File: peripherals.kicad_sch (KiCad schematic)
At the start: 53 parts, among them J10 533980471, J11 ERF8-040-05.0-L-DV-K-TR, J7 FC Conn, J9 TC2050-IDC-NL, Q10 PJE138K, Q9 PJE138K, U30 TPD4E05U06QDQARQ1, U33 NTS0102GT, U34 PCAL6408ABSHP

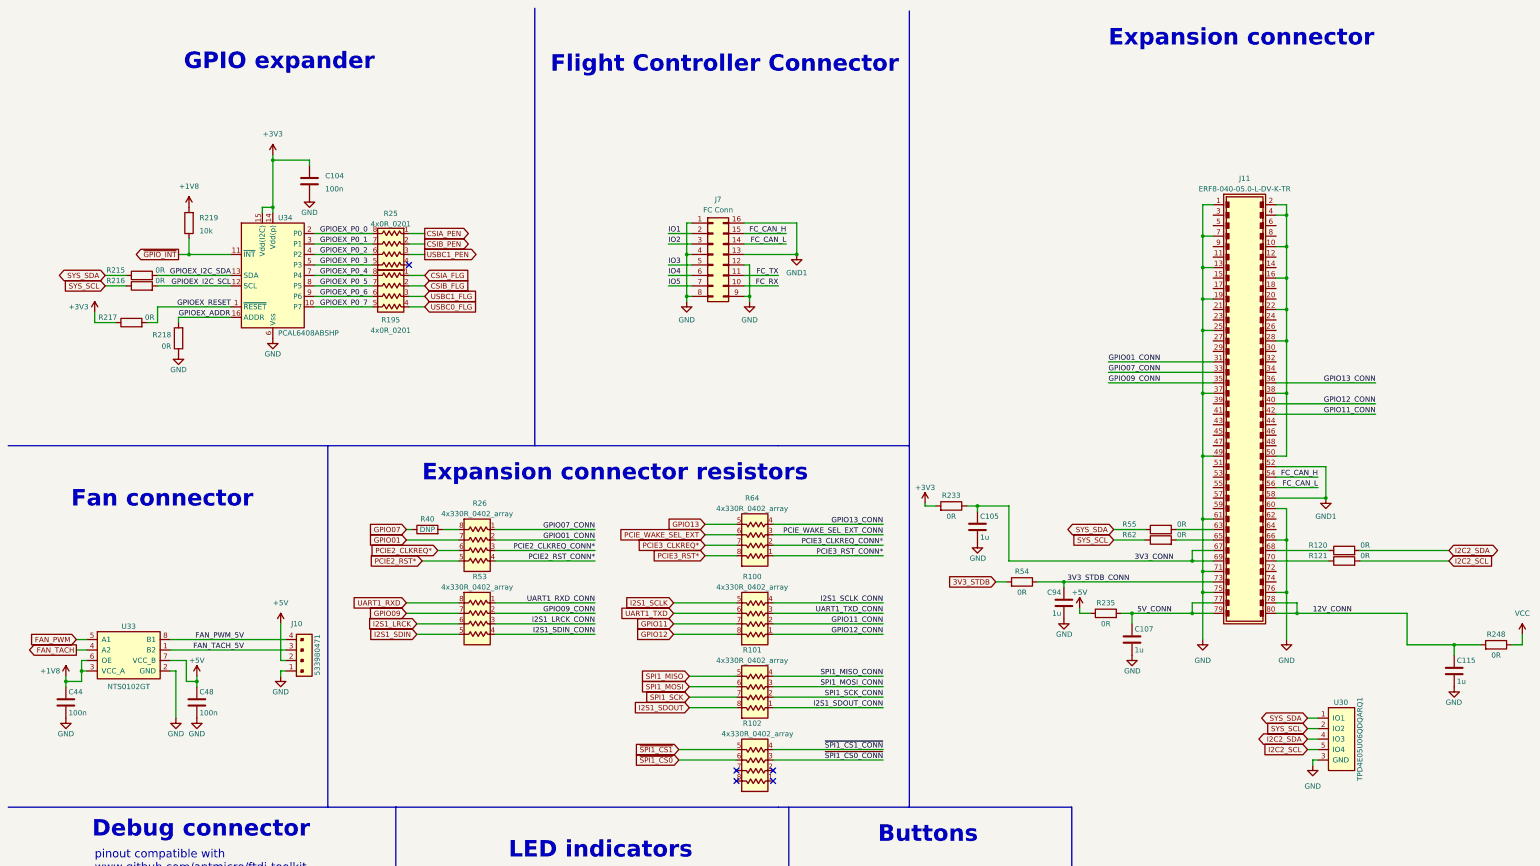
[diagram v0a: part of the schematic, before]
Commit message: Reducing pin count to 30
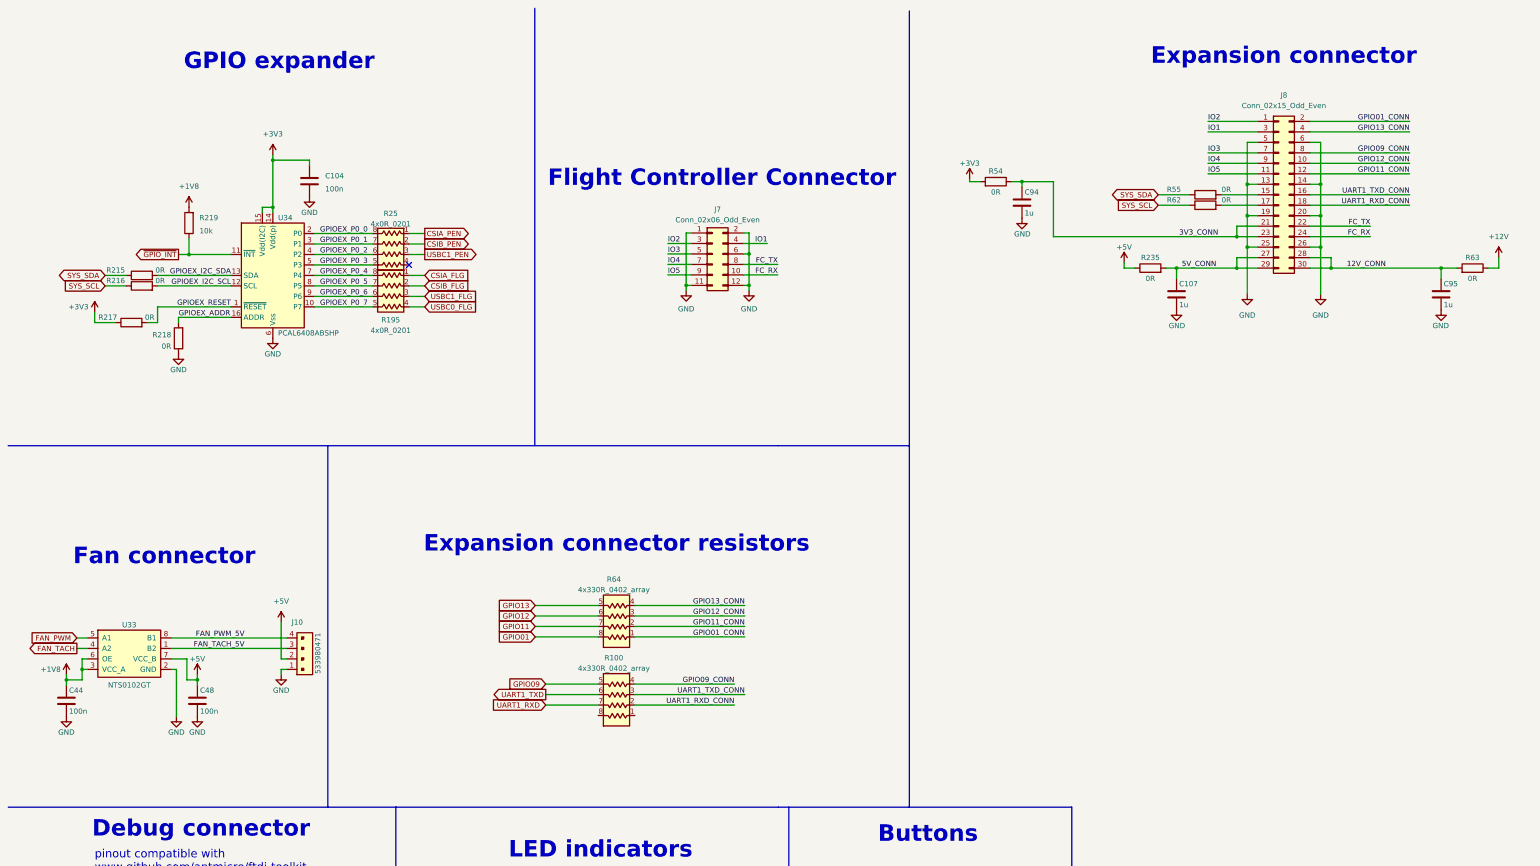
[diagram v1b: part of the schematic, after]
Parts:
- removed C105, C115: C_1u_0402, jetson-orin-baseboard-footprints:0402-cap, symbol jetson-orin-baseboard:C_1u_0402
- removed J11: ERF8-040-05.0-L-DV-K-TR, jetson-orin-baseboard-footprints:ERF8-040-XX.X-X-DV-XX, symbol jetson-orin-baseboard:ERF8-040-05.0-L-DV-K-TR
- removed J7: FC Conn, symbol Connector_Generic:Conn_02x08_Counter_Clockwise
- removed R101, R102, R26, R53: 4x330R_0402_array, jetson-orin-baseboard-footprints:R_Array_4x0402, symbol jetson-orin-baseboard:4x330R_0402_array
- removed R120, R121: R_0R_0402, jetson-orin-baseboard-footprints:0402-res, symbol jetson-orin-baseboard:R_0R_0402
- removed R233, R248: R_0R_0603, jetson-orin-baseboard-footprints:0603-res, symbol jetson-orin-baseboard:R_0R_0603
- removed R40: DNP, symbol Device:R
- removed U30: TPD4E05U06QDQARQ1, jetson-orin-baseboard-footprints:USON-10_2.5x1.0mm_P0.5mm, symbol jetson-orin-baseboard:TPD4E05U06QDQARQ1
- added C95: C_1u_0402, jetson-orin-baseboard-footprints:0402-cap, symbol jetson-orin-baseboard:C_1u_0402
- added J7: Conn_02x06_Odd_Even, symbol Connector_Generic:Conn_02x06_Odd_Even
- added J8: Conn_02x15_Odd_Even, symbol Connector_Generic:Conn_02x15_Odd_Even
- added R63: R_0R_0603, jetson-orin-baseboard-footprints:0603-res, symbol jetson-orin-baseboard:R_0R_0603
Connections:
- net 3V3_STDB is gone; now on net +3V3: R54.2
- net 3V3_STDB_CONN is gone; now on net 3V3_CONN: C94.1, R54.1
- net I2S1_SCLK is gone; now on net GPIO09: R100.5
- net I2S1_SCLK_CONN is gone; now on net GPIO09_CONN: R100.4
- net PCIE3_CLKREQ* is gone; now on net GPIO11: R64.7
- net PCIE3_CLKREQ_CONN* is gone; now on net GPIO11_CONN: R64.2
- net PCIE3_RST* is gone; now on net GPIO01: R64.8
- net PCIE3_RST_CONN* is gone; now on net GPIO01_CONN: R64.1
- net PCIE_WAKE_SEL_EXT is gone; now on net GPIO12: R64.6
- net PCIE_WAKE_SEL_EXT_CONN is gone; now on net GPIO12_CONN: R64.3
- net 12V_CONN: now also C95.1, J8.28 (Pin_28), J8.30 (Pin_30), R63.2
- net 3V3_CONN: now also J8.21 (Pin_21), J8.23 (Pin_23)
- net 5V_CONN: now also J8.27 (Pin_27), J8.29 (Pin_29)
- net FC_RX: now also J7.10 (Pin_10), J8.24 (Pin_24)
- net FC_TX: now also J7.8 (Pin_8), J8.22 (Pin_22)
- net GND: now also C95.2, J7.1 (Pin_1), J7.11 (Pin_11), J7.12 (Pin_12), J7.2 (Pin_2), J7.6 (Pin_6), J8.13 (Pin_13), J8.14 (Pin_14), J8.19 (Pin_19), J8.20 (Pin_20), J8.25 (Pin_25), J8.26 (Pin_26), J8.5 (Pin_5), J8.6 (Pin_6)
- net GPIO01_CONN: now also J8.2 (Pin_2)
- net GPIO09_CONN: now also J8.8 (Pin_8)
- net GPIO11: no longer R100.7
- net GPIO11_CONN: now also J8.12 (Pin_12); no longer R100.2
- net GPIO12: no longer R100.8
- net GPIO12_CONN: now also J8.10 (Pin_10); no longer R100.1
- net GPIO13_CONN: now also J8.4 (Pin_4)
- net IO1: now also J7.4 (Pin_4), J8.3 (Pin_3)
- net IO2: now also J7.3 (Pin_3), J8.1 (Pin_1)
- net IO3: now also J7.5 (Pin_5), J8.7 (Pin_7)
- net IO4: now also J7.7 (Pin_7), J8.9 (Pin_9)
- net IO5: now also J7.9 (Pin_9), J8.11 (Pin_11)
- net UART1_RXD: now also R100.7
- net UART1_RXD_CONN: now also R100.2, J8.18 (Pin_18)
- net UART1_TXD_CONN: now also J8.16 (Pin_16)
- net at R62.2: now also J8.17 (Pin_17)
- net at R55.2: now also J8.15 (Pin_15)
- new net +12V: R63.1
- no-connect marks 6 -> 2
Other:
- moved on the sheet: C107, R100, R235, R64

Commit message: Schematic check
Include Pinmux and Schematic Check excels in doc folder and doing a lot of checking and correcting things.
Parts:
- removed C104: C_100n_0402, jetson-orin-baseboard-footprints:0402-cap, symbol jetson-orin-baseboard:C_100n_0402
- removed R100: 4x330R_0402_array, jetson-orin-baseboard-footprints:R_Array_4x0402, symbol jetson-orin-baseboard:4x330R_0402_array
- removed R195, R25: 4x0R_0201_array, jetson-orin-baseboard-footprints:EXB18V, symbol jetson-orin-baseboard:4x0R_0201_array
- removed R215, R216, R217, R218: R_0R_0402, jetson-orin-baseboard-footprints:0402-res, symbol jetson-orin-baseboard:R_0R_0402
- removed R219: R_10k_0402, jetson-orin-baseboard-footprints:0402-res, symbol jetson-orin-baseboard:R_10k_0402
- removed U34: PCAL6408ABSHP, jetson-orin-baseboard-footprints:VQFN-16-1EP_3x3mm, symbol jetson-orin-baseboard:PCAL6408ABSHP
- added C42, C43: 100n, symbol Device:C
- added C79: 0.1u, symbol Device:C
- added C80: 2.2u, symbol Device:C
- added C81: 10n, symbol Device:C
- added C82: 0.47u, symbol Device:C
- added C88: C_1u_0402, jetson-orin-baseboard-footprints:0402-cap, symbol jetson-orin-baseboard:C_1u_0402
- added D14, D15, D16, D17: TPD1E0B04DPYR, jetson-orin-baseboard-footprints:XDFN-2_1x0.60mm, symbol jetson-orin-baseboard:TPD1E0B04DPYR
- added R1: R_0R_0603, jetson-orin-baseboard-footprints:0603-res, symbol jetson-orin-baseboard:R_0R_0603
- added R2: 0, symbol Device:R
- added U2: ICM-20602, Package_LGA:LGA-16_3x3mm_P0.5mm_LayoutBorder3x5y, symbol Sensor_Motion:ICM-20602
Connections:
- net GPIO09_CONN is gone; now on net FC_TX: J8.8 (Pin_8)
- net GPIO11 is gone; now on net UART1_RXD: R64.7
- net GPIO12 is gone; now on net UART1_TXD: R64.6
- net +1V8: now also C79.1, C80.1, R1.2, U2.16 (VDD)
- net 3V3_CONN: no longer J8.23 (Pin_23)
- net FC_RX: now also J8.10 (Pin_10); no longer J8.24 (Pin_24)
- net FC_TX: no longer J8.22 (Pin_22)
- net GND: now also C79.2, C80.2, C81.2, C82.2, C88.2, D14.2, D15.2, D16.2, D17.2, U2.10 (GND), U2.11 (GND), U2.12 (GND), U2.13 (GND), U2.15 (GND), U2.8 (FSYNC), U2.9 (GND)
- net GPIO09: now also R2.2
- net GPIO13_CONN: now also J8.12 (Pin_12); no longer J8.4 (Pin_4), R64.4
- net UART1_RXD_CONN: now also J8.4 (Pin_4), R64.2; no longer J8.18 (Pin_18)
- net UART1_TXD_CONN: now also J8.2 (Pin_2), R64.3; no longer J8.16 (Pin_16)
- net GPIO01: no longer names the net of R64.8
- net GPIO01_CONN: no longer names the net of R64.1
- net GPIO01_CONN: no longer J8.2 (Pin_2)
- removed net GPIO11_CONN: J8.12 (Pin_12), R64.2
- removed net GPIO12_CONN: J8.10 (Pin_10), R64.3
- net GPIO13 renamed GPIO_PAC
- new net: C81.1, U2.1 (VDDIO)
- new net: C82.1, U2.14 (REGOUT)
- new net: R2.1, U2.6 (INT)
- new net 1V8_CONN: C88.1, J8.23 (Pin_23), R1.1
- new net GPIO_PAC_CONN: R64.4
- new net SPIO_MISO: U2.4 (SAO/SD0)
- new net SPIO_MOSI: U2.3 (SDA/SDI)
- new net SPIO_SCK: U2.2 (SCL/SPC)
- new net USBSS1_RX_N: D14.1, J8.24 (Pin_24)
- new net USBSS1_RX_P: D15.1, J8.22 (Pin_22)
- new net USBSS1_TX_N: C43.2
- new net USBSS1_TX_N_CONN: C43.1, D17.1, J8.18 (Pin_18)
- new net USBSS1_TX_P: C42.2
- new net USBSS1_TX_P_CONN: C42.1, D16.1, J8.16 (Pin_16)
- new net ~{SPI0_CS0}: U2.5 (~{CS})
- no-connect marks 2 -> 1
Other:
- note added: "IMU"
- note added: "SYS I2C Addresses in Use -0100011 for Port 1 of I2C1 of TPS65988 (CONFIGURABLE) -0100111 for Port 2 of I2C1 of TPS65988 (CONFIGURABLE) -0010010 for TUSB1046-DCI (I2C UNUSED, CONFIGURABLE) -1X00111 for HD3SS3220(I2C UNUSED, 2 CHOICE) -010000X for planned PCAL6408A on PAC PCB (2 CHOICE) -1000000 for power monitor on module"
- note removed: "GPIO expander"
- moved on the sheet: C107, C94, C95, J8, R235, R54, R55, R62, R63, R64

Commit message: Small changes
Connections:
- net GPIO13_CONN is gone; now on net GPIO_PAC_CONN: J8.12 (Pin_12)
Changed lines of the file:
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@@
     (effects (font (size 1.27 1.27)) (justify left bottom))
   )
-  (label "GPIO13_CONN" (at 353.06 53.34 180) (fields_autoplaced)
+  (label "GPIO_PAC_CONN" (at 353.06 53.34 180) (fields_autoplaced)
     (effects (font (size 1.27 1.27)) (justify right bottom))
   )
@@
     )
   )
-  (global_label "GPIO_PAC" (shape input) (at 140.97 157.48 180) (fields_autoplaced)
+  (global_label "GPIO_PAC" (shape output) (at 140.97 157.48 180) (fields_autoplaced)
     (effects (font (size 1.27 1.27)) (justify right))
     (property "Intersheetrefs" "${INTERSHEET_REFS}" (at 128.9133 157.48 0)
@@
   (symbol (lib_id "power:GND") (at 78.105 91.44 0) (unit 1)
     (in_bom yes) (on_board yes) (dnp no) (fields_autoplaced)
-    (property "Reference" "#PWR015" (at 78.105 97.79 0)
+    (property "Reference" "#PWR020" (at 78.105 97.79 0)
       (effects (font (size 1.27 1.27)) hide)
     )
@@
   (symbol (lib_id "power:GND") (at 93.98 60.325 0) (unit 1)
     (in_bom yes) (on_board yes) (dnp no) (fields_autoplaced)
-    (property "Reference" "#PWR024" (at 93.98 66.675 0)
+    (property "Reference" "#PWR021" (at 93.98 66.675 0)
       (effects (font (size 1.27 1.27)) hide)
     )
@@
   (symbol (lib_id "power:GND") (at 62.23 64.135 0) (unit 1)
     (in_bom yes) (on_board yes) (dnp no) (fields_autoplaced)
-    (property "Reference" "#PWR023" (at 62.23 70.485 0)
-      (effects (font (size 1.27 1.27)) hide)
-    )
+    (property "Reference" "#PWR015" (at 62.23 70.485 0)
+      (effects (font (size 1.27 1.27)) hide)
+    )

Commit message: Schematic Done
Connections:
- no-connect marks 1 -> 3
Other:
- moved on the sheet: C107, C43, C44, C48, C79, C80, C81, C82, C94, D14, D15, D16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

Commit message: Schematic V1 and footprints assigned
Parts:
- removed J7: Conn_02x06_Odd_Even, symbol Connector_Generic:Conn_02x06_Odd_Even
- removed J8: Conn_02x15_Odd_Even, symbol Connector_Generic:Conn_02x15_Odd_Even
- added J10: 532611071, jetson-orin-baseboard-footprints:MOLEX_532611071, symbol 532611071:532611071
- added J11: ERF8-020-05.0-S-DV-L-TR, jetson-orin-baseboard-footprints:ERF8-040-XX.X-X-DV-XX, symbol ERF8-020-05.0-S-DV-L-TR:ERF8-020-05.0-S-DV-L-TR
- C79: footprint (none) -> jetson-orin-baseboard-footprints:0402-cap
- C81: renamed from C80; footprint (none) -> jetson-orin-baseboard-footprints:0402-cap
- C82: renamed from C81; footprint (none) -> jetson-orin-baseboard-footprints:0402-cap
- C83: renamed from C82; footprint (none) -> jetson-orin-baseboard-footprints:0402-cap
- C87: renamed from C42; footprint (none) -> jetson-orin-baseboard-footprints:0402-cap
- C89: renamed from C43; footprint (none) -> jetson-orin-baseboard-footprints:0402-cap
- R106: renamed from R2; footprint (none) -> jetson-orin-baseboard-footprints:0402-res
- renumbered C44 to C78, C48 to C80, C94 to C84, C88 to C85, C107 to C86, C95 to C88, D26 to D37, D27 to D38, D58 to D39, D59 to D40, D14 to D41, D15 to D42, D16 to D43, D17 to D44, J9 to J8, J10 to J9, Q9 to Q4, Q10 to Q5, R111 to R103, R112 to R104, R204 to R105, R222 to R107, R223 to R108, R64 to R109, R230 to R110, R231 to R111, R232 to R112, R242 to R113, R54 to R114, R1 to R115, R235 to R116, R55 to R117, R62 to R118, R63 to R119, U33 to U20, U2 to U21
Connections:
- net 12V_CONN: now also J11.32, J11.34, J11.36, J11.38
- net 1V8_CONN: now also J11.02, J11.04
- net 3V3_CONN: now also J11.33, J11.35, J11.37
- net 5V_CONN: now also J11.01, J11.03, J11.05, J11.07
- net FC_RX: now also J10.3, J11.16
- net FC_TX: now also J10.2, J11.14
- net GND: now also J10.1, J10.4, J10.8, J10.S1 (SHIELD1), J10.S2 (SHIELD2), J11.06, J11.09, J11.12, J11.17, J11.18, J11.24, J11.25, J11.30, J11.31, J11.39, J11.40
- net GPIO_PAC_CONN: now also J11.23
- net IO1: now also J10.5, J11.13
- net IO2: now also J10.6, J11.11
- net IO3: now also J10.7, J11.15
- net IO4: now also J10.9, J11.19
- net IO5: now also J10.10, J11.21
- net UART1_RXD_CONN: now also J11.10
- net UART1_TXD_CONN: now also J11.08
- net USBSS1_RX_N: now also J11.28
- net USBSS1_RX_P: now also J11.26
- net USBSS1_TX_N_CONN: now also J11.22
- net USBSS1_TX_P_CONN: now also J11.20
- net at R118.2: now also J11.29
- net at R117.2: now also J11.27
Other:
- moved on the sheet: C84, C85, C86, C87, C88, C89, R114, R115, R116, R117, R118, R119
